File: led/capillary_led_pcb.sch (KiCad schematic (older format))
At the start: 17 parts, among them P1 CONN_2

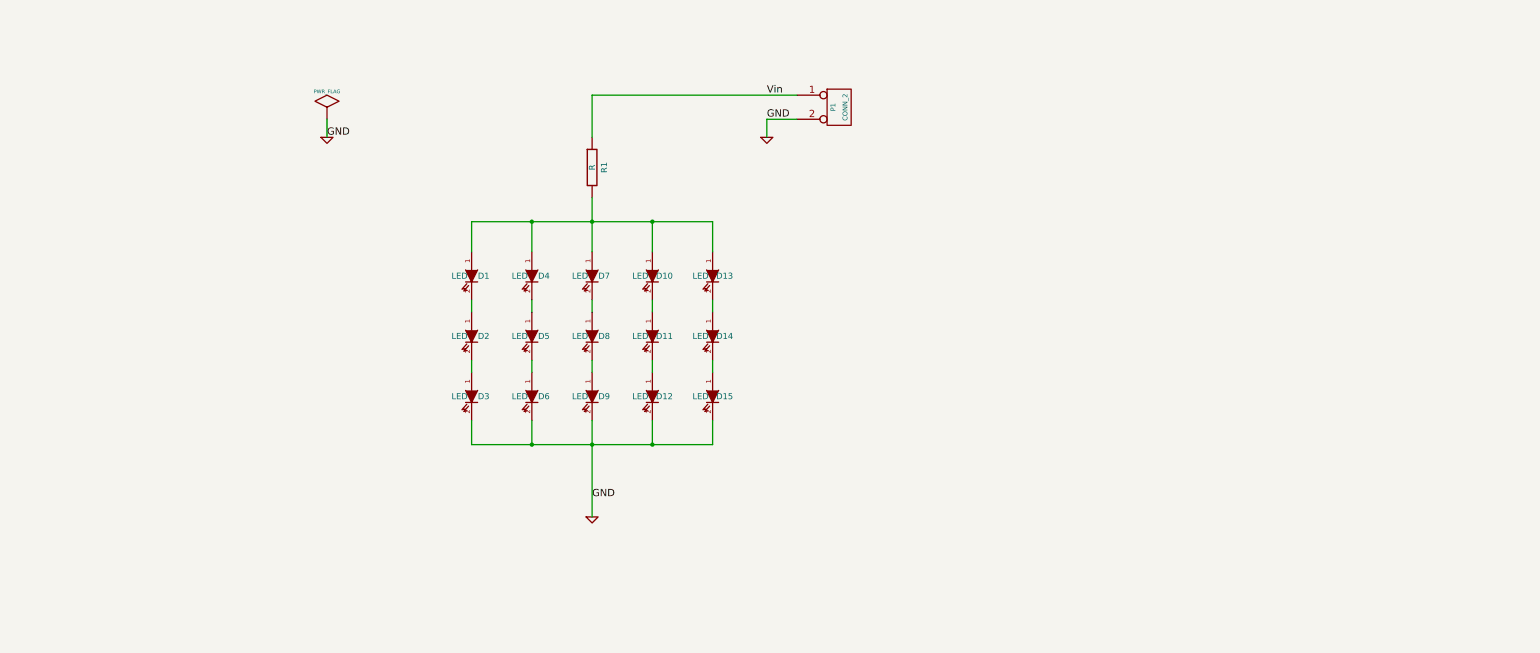
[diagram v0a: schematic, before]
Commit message: Added five channel led pcb.
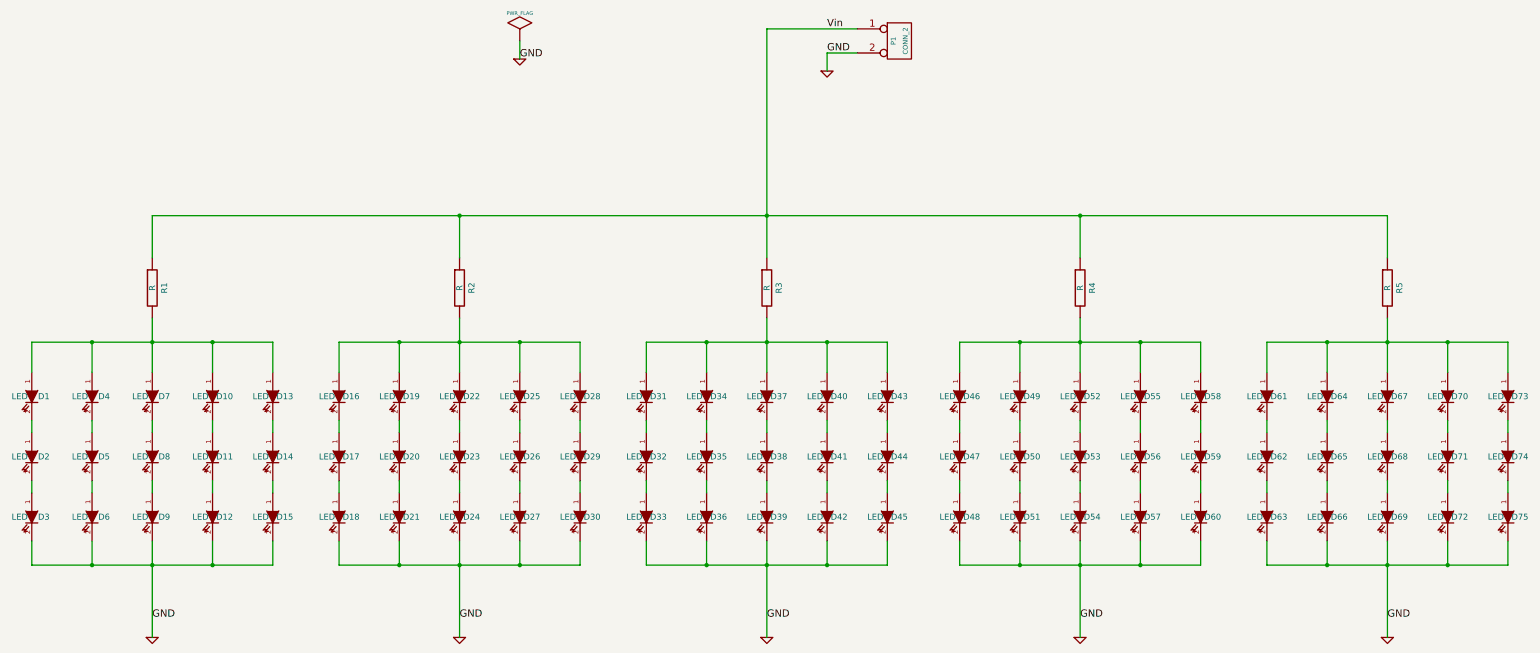
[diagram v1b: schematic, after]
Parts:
- added D16, D17, D18, D19, D20, D21, D22, D23, D24, D25, D26, D27, D28, D29, D30, D31, D32, D33, D34, D35, D36, D37, D38, D39, D40, D41, D42, D43, D44, D45, D46, D47, D48, D49, D50, D51, D52, D53, D54, D55, D56, D57, D58, D59, D60, D61, D62, D63, D64, D65, D66, D67, D68, D69, D70, D71, D72, D73, D74, D75: LED, symbol LED
- added R2, R3, R4, R5: R, symbol R
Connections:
- net GND: now also D18.2 (K), D21.2 (K), D24.2 (K), D27.2 (K), D30.2 (K), D33.2 (K), D36.2 (K), D39.2 (K), D42.2 (K), D45.2 (K), D48.2 (K), D51.2 (K), D54.2 (K), D57.2 (K), D60.2 (K), D63.2 (K), D66.2 (K), D69.2 (K), D72.2 (K), D75.2 (K)
- net Vin: now also R2.1, R3.1, R4.1, R5.1
- new net: D16.1 (A), D19.1 (A), D22.1 (A), D25.1 (A), D28.1 (A), R2.2
- new net: D29.2 (K), D30.1 (A)
- new net: D28.2 (K), D29.1 (A)
- new net: D26.2 (K), D27.1 (A)
- new net: D25.2 (K), D26.1 (A)
- new net: D23.2 (K), D24.1 (A)
- new net: D22.2 (K), D23.1 (A)
- new net: D20.2 (K), D21.1 (A)
- new net: D19.2 (K), D20.1 (A)
- new net: D17.2 (K), D18.1 (A)
- new net: D16.2 (K), D17.1 (A)
- new net: D46.1 (A), D49.1 (A), D52.1 (A), D55.1 (A), D58.1 (A), R4.2
- new net: D46.2 (K), D47.1 (A)
- new net: D47.2 (K), D48.1 (A)
- new net: D49.2 (K), D50.1 (A)
- new net: D50.2 (K), D51.1 (A)
- new net: D52.2 (K), D53.1 (A)
- new net: D53.2 (K), D54.1 (A)
- new net: D55.2 (K), D56.1 (A)
- new net: D56.2 (K), D57.1 (A)
- new net: D58.2 (K), D59.1 (A)
- new net: D59.2 (K), D60.1 (A)
- new net: D31.1 (A), D34.1 (A), D37.1 (A), D40.1 (A), D43.1 (A), R3.2
- new net: D44.2 (K), D45.1 (A)
- new net: D43.2 (K), D44.1 (A)
- new net: D41.2 (K), D42.1 (A)
- new net: D40.2 (K), D41.1 (A)
- new net: D38.2 (K), D39.1 (A)
- new net: D37.2 (K), D38.1 (A)
- new net: D35.2 (K), D36.1 (A)
- new net: D34.2 (K), D35.1 (A)
- new net: D32.2 (K), D33.1 (A)
- new net: D31.2 (K), D32.1 (A)
- new net: D61.1 (A), D64.1 (A), D67.1 (A), D70.1 (A), D73.1 (A), R5.2
- new net: D74.2 (K), D75.1 (A)
- new net: D73.2 (K), D74.1 (A)
- new net: D71.2 (K), D72.1 (A)
- new net: D70.2 (K), D71.1 (A)
- new net: D68.2 (K), D69.1 (A)
- new net: D67.2 (K), D68.1 (A)
- new net: D65.2 (K), D66.1 (A)
- new net: D64.2 (K), D65.1 (A)
- new net: D62.2 (K), D63.1 (A)
- new net: D61.2 (K), D62.1 (A)
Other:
- moved on the sheet: D1, D10, D11, D12, D13, D14, D15, D2, D3, D4, D5, D6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

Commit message: Swapped names for led and led_five_chan.
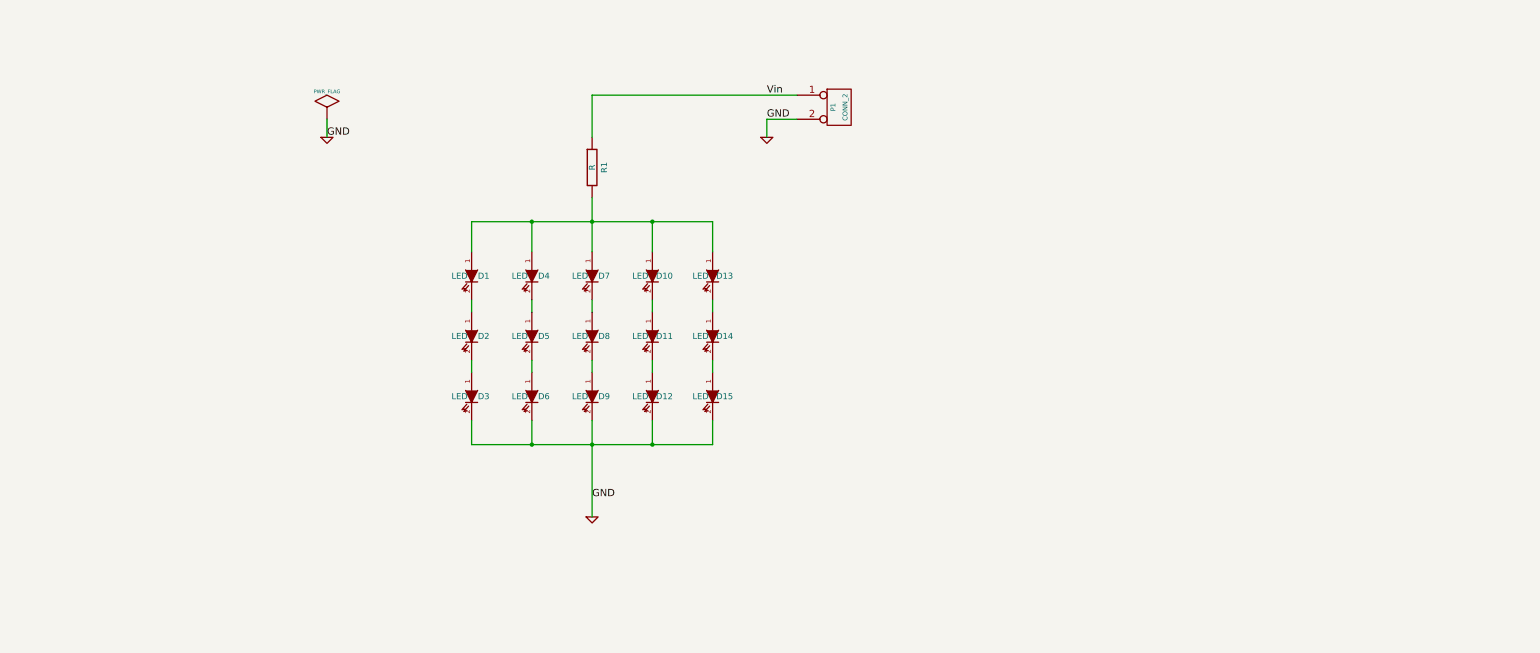
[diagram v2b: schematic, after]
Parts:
- removed D16, D17, D18, D19, D20, D21, D22, D23, D24, D25, D26, D27, D28, D29, D30, D31, D32, D33, D34, D35, D36, D37, D38, D39, D40, D41, D42, D43, D44, D45, D46, D47, D48, D49, D50, D51, D52, D53, D54, D55, D56, D57, D58, D59, D60, D61, D62, D63, D64, D65, D66, D67, D68, D69, D70, D71, D72, D73, D74, D75: LED, symbol LED
- removed R2, R3, R4, R5: R, symbol R
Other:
- moved on the sheet: D1, D10, D11, D12, D13, D14, D15, D2, D3, D4, D5, D6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
